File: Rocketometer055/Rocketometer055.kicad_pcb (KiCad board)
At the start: 2 copper layers, 26.7 x 20.3 mm, 31 parts, among them Q1 BSS138, Q2 BSS138, U1 MIC5225, Y1 32.768kHz

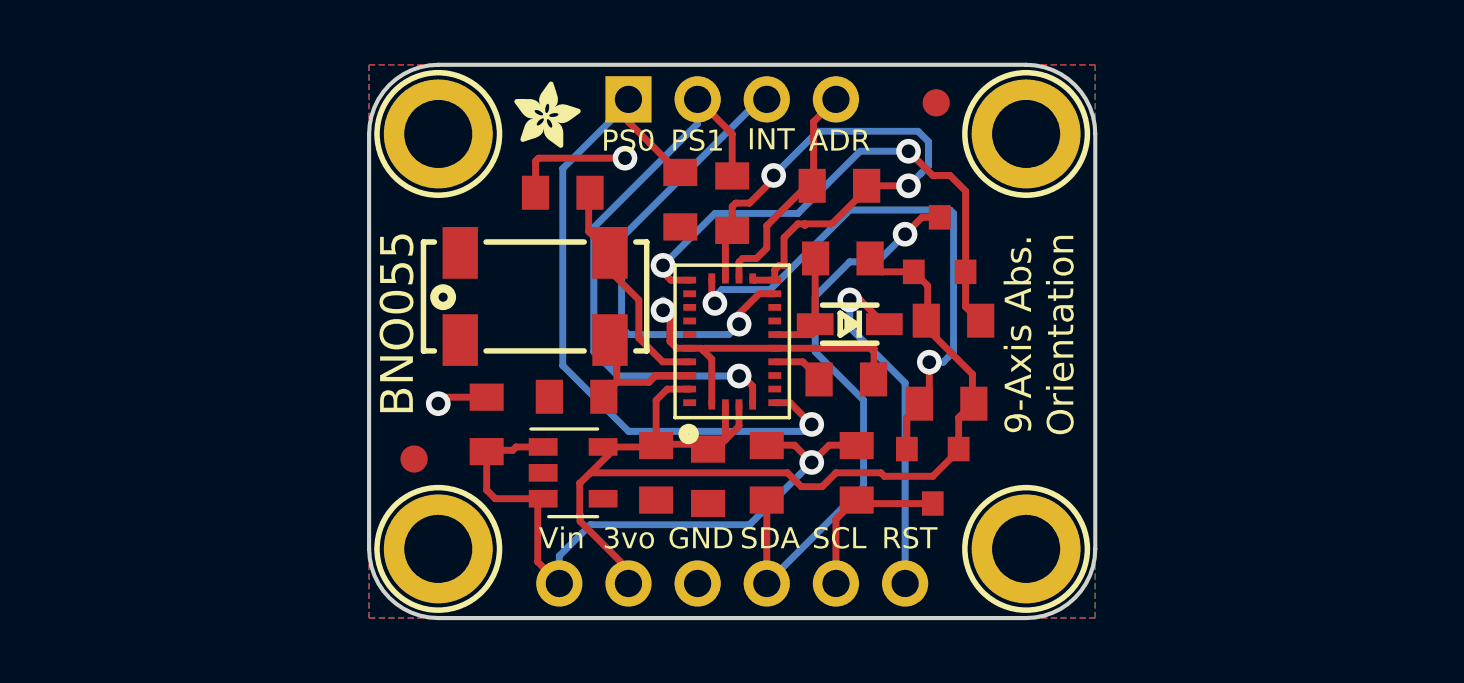
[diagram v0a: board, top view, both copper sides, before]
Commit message: Importing Rocketometer6050 as flown
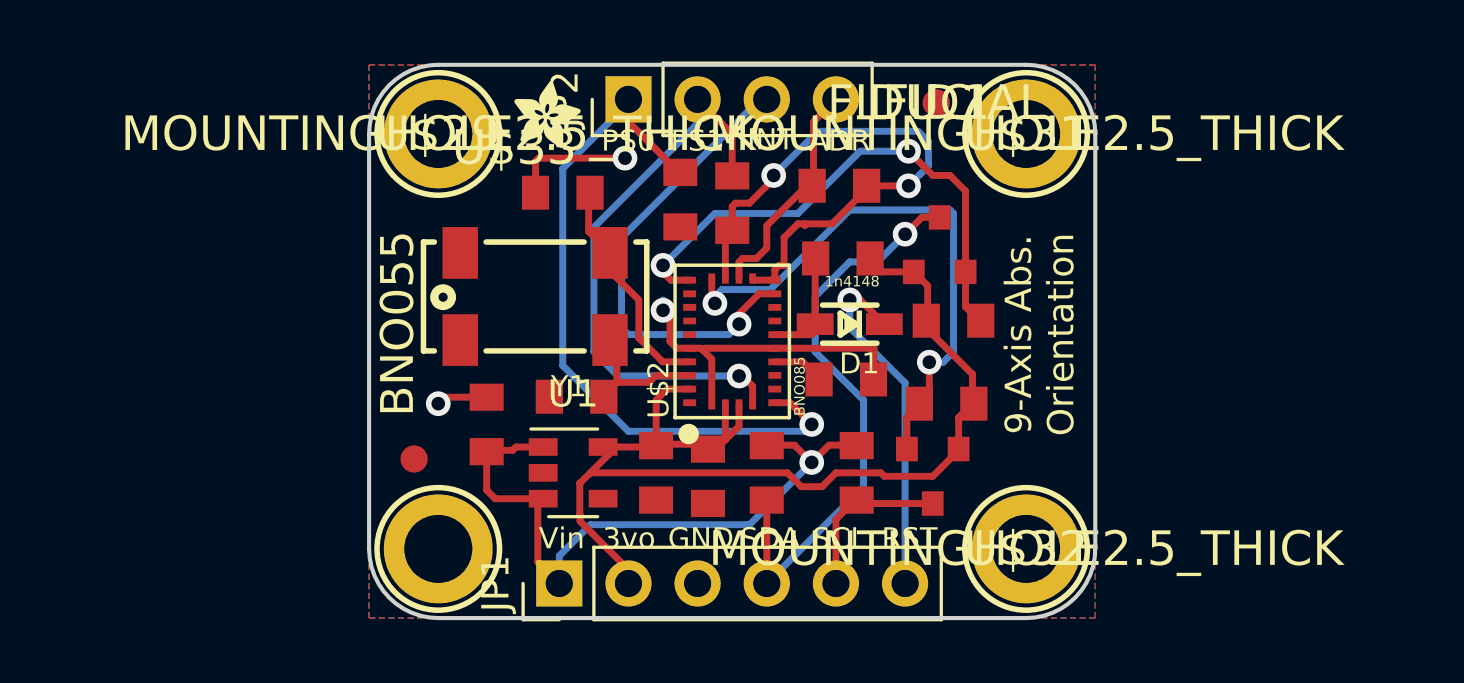
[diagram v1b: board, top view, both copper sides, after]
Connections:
- net /BMO055/N$1 renamed /N$1
- net /BMO055/N$2 renamed /N$2
- net /BMO055/N$3 renamed /N$3
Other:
- net class Default: clearance 0 -> 0.1524
- rule trace_clearance: 0 -> 0.1524

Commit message: Worked on Rocketometer055
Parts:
- removed C1, C2: 22pF, KwanSystems:SMD_0805
- removed C3, C4: 0.1uF, KwanSystems:SMD_0805
- removed C5, C6: 10uF, KwanSystems:SMD_0805
- removed D1: 1n4148, KwanSystems:SOD-323
- removed FID1, FID2: FIDUCIAL, FIDUCIAL_1MM
- removed Q1, Q2: BSS138, KwanSystems:SOT-23
- removed R10, R3, R4, R5, R6, R7, R8, R9: 10K, KwanSystems:SMD_0805
- removed U$2: BNO085, KwanSystems:BNO055
- removed U$28: , ADAFRUIT_TEXT_20MM
- removed U$29, U$30, U$31, U$32: MOUNTINGHOLE2.5_THICK, MOUNTINGHOLE_2.5_PLATED_THICK
- removed U$3: , PCBFEAT-REV-040
- removed U$33: , ADAFRUIT_2.5MM
- removed U1: MIC5225, TO_SOT_Packages_SMD:SOT-23-5
- removed Y1: 32.768kHz, KwanSystems:CRYSTAL_8X3.8
- added B504: Coin_Cell, KwanSystems:CR1220-2, F.Cu at (164.1, 91.7)
- added C010: 1uF, KwanSystems:SMD_0402, F.Cu at (264.9, 116.1)
- added C020: 22pF, KwanSystems:SMD_0402, F.Cu at (258.5, 114.4)
- added C023: 22pF, KwanSystems:R_Array_Convex_2x0402, F.Cu at (176.9, 85.3)
- added C030: 22pF, KwanSystems:SMD_0402, F.Cu at (260.9, 111.0)
- added C106: 100nF, KwanSystems:R_Array_Convex_2x0402, F.Cu at (150.1, 83.7)
- added C204: 1uF, KwanSystems:SMD_0402, F.Cu at (253.0, 110.7)
- added C214: 100nF, KwanSystems:SMD_0402, F.Cu at (252.5, 121.5)
- added C215: 4.7nF, KwanSystems:SMD_0402, F.Cu at (249.0, 123.1)
- added C302: 4.7uF, KwanSystems:SMD_0603, F.Cu at (253.5, 114.3)
- added C303: 4.7uF, KwanSystems:SMD_0603, F.Cu at (175.0, 96.3)
- added C423: 1uF, KwanSystems:SMD_0402, B.Cu at (157.0, 100.8)
- added C443: 100nF, KwanSystems:SMD_0402, B.Cu at (149.9, 93.0)
- added C451: 100nF, KwanSystems:SMD_0402, B.Cu at (152.7, 87.0)
- added C461: 33pF, KwanSystems:SMD_0402, B.Cu at (158.5, 82.8)
- added C462: 33pF, KwanSystems:SMD_0402, B.Cu at (161.8, 85.6)
- added C463: 100nF, KwanSystems:SMD_0402, B.Cu at (162.1, 88.1)
- added C501: 100nF, KwanSystems:SMD_0402, F.Cu at (171.5, 136.9)
- added C503: 10uF, KwanSystems:SMD_1206, F.Cu at (187.3, 124.7)
- added C504: 220mF, KwanSystems:Supercap, F.Cu at (212.4, 114.1)
- added C603: 0.1uF, KwanSystems:SMD_0402, F.Cu at (174.7, 147.7)
- added C609: 0.1uF, KwanSystems:SMD_0402, F.Cu at (170.2, 148.6)
- added C626: 22pF, KwanSystems:SMD_0402, F.Cu at (155.2, 91.4)
- added C627: 22pF, KwanSystems:SMD_0402, F.Cu at (155.4, 87.4)
- added C901: 100nF, KwanSystems:SMD_0402, F.Cu at (184.5, 142.1)
- added C914: 100nF, KwanSystems:SMD_0402, F.Cu at (184.5, 143.3)
- added C916: 1uF, KwanSystems:SMD_0402, F.Cu at (186.9, 142.1)
- added D050: BLUE, KwanSystems:D_0603, F.Cu at (179.6, 85.3)
- added D301: YELLOW, KwanSystems:D_0603, F.Cu at (249.5, 121.7)
- added D302: DCC, KwanSystems:SOT-23, F.Cu at (175.0, 93.7)
- added D401: HSMF-C118, KwanSystems:HSMF-C118, B.Cu at (167.1, 81.8)
- added D504: D_Schottky, KwanSystems:D_0603, F.Cu at (168.3, 137.1)
- added J001: USB_MICROB, KwanSystems:USB_Micro-B_Molex_47346-0001, F.Cu at (182.9, 90.2)
- added J301: JST 2mm, Connectors_JST:JST_PH_S2B-PH-SM4-TB_02x2.00mm_Angled, B.Cu at (178.3, 90.2)
- added J401: ~, Pin_Headers:Pin_Header_Straight_1x10_Pitch2.54mm, F.Cu at (163.8, 80.0)
- added J701: Micro_SD_Card_Det_Hirose_DM3AT, KwanSystems:MICROSD-SOCKET-PP, F.Cu at (132.6, 84.2)
- added JP4: STAND-OFFTIGHT, STAND-OFF-TIGHT, F.Cu at (180.3, 99.1)
- added JP5: STAND-OFFTIGHT, STAND-OFF-TIGHT, F.Cu at (180.3, 81.3)
- added L501: Ferrite, KwanSystems:SMD_0805, F.Cu at (175.7, 130.1)
- added Q050: PMOS, KwanSystems:SOT-23, F.Cu at (174.2, 84.1)
- added R010: 10k, KwanSystems:SMD_0402, F.Cu at (177.8, 95.5)
- added R011: 22k, KwanSystems:SMD_0402, F.Cu at (254.8, 121.5)
- added R023: 33, KwanSystems:R_Array_Convex_2x0402, F.Cu at (176.9, 87.4)
- added R050: 1.5k, KwanSystems:R_Array_Convex_2x0402, F.Cu at (176.9, 83.3)
- added R051: 10k, KwanSystems:SMD_0402, F.Cu at (251.4, 123.9)
- added R301: 10k, KwanSystems:SMD_0402, F.Cu at (254.8, 122.7)
- added R302: 1.5k, KwanSystems:SMD_0402, F.Cu at (253.5, 113.0)
- added R304: 1.5k, KwanSystems:SMD_0402, F.Cu at (177.8, 96.5)
- added R401: 10k, KwanSystems:R_Array_Convex_4x0402, B.Cu at (151.9, 85.1)
- added R402: 1.5k, KwanSystems:R_Array_Convex_4x0402, B.Cu at (169.7, 81.8)
- added R504: 10k, KwanSystems:SMD_0402, F.Cu at (206.3, 122.8)
- added R914: 100, KwanSystems:SMD_0402, F.Cu at (186.9, 143.3)
- added S201: SPDT, KwanSystems:SWITCH_DPDT_AZY0202, B.Cu at (172.5, 97.8)
- added S456: SOLDERJUMPERNO, Connectors:GS2, B.Cu at (155.3, 82.8)
- added S457: SPST, KwanSystems:SW_SPST_B3U-1000P, B.Cu at (155.4, 85.6)
- added U101: BME280, KwanSystems:BME280, F.Cu at (152.7, 83.9)
- added U201: 3.3V, TO_SOT_Packages_SMD:SOT-23-5, F.Cu at (250.0, 110.8)
- added U301: MCP73831, TO_SOT_Packages_SMD:SOT-23-5, F.Cu at (175.0, 90.2)
- added U401: LPC2148, Housings_QFP:LQFP-64_10x10mm_Pitch0.5mm, B.Cu at (156.8, 93.9)
- added U501: FGPMMOPA6H, KwanSystems:FGPMMOPA6H, B.Cu at (140.5, 90.6)
- added U501: MPU9250, KwanSystems:Axis, F.Cu at (175.3, 100.3)
- added U601: BNO085, KwanSystems:BNO055, F.Cu at (152.4, 90.2)
- added U901: ADXL375, KwanSystems:ADXL375, F.Cu at (153.3, 98.4)
- added X511: uFL, KwanSystems:U.FL, B.Cu at (129.5, 92.5)
- added Y401: 12MHz, Crystals:Crystal_SMD_Abracon_ABM8G-4pin_3.2x2.5mm, B.Cu at (159.4, 85.5)
- added Y601: 32kiHz, Crystals:Crystal_SMD_2012-2pin_2.0x1.2mm, F.Cu at (155.2, 89.2)
- JP1: value ~ -> STAND-OFFTIGHT; footprint Pin_Headers:Pin_Header_Straight_1x06_Pitch2.54mm -> STAND-OFF-TIGHT
- JP2: value ~ -> STAND-OFFTIGHT; footprint Pin_Headers:Pin_Header_Straight_1x04_Pitch2.54mm -> STAND-OFF-TIGHT
- moved JP2 7.10 mm to (129.5, 81.3), turned to 0 degrees
- moved JP1 4.62 mm to (129.5, 99.1), turned to 0 degrees
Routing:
- net GND: track 41.0 -> 0.00 mm, vias 5 -> 0
- net +3V3: track 40.6 -> 0.00 mm
- net /PS0_3V: track 26.2 -> 0.00 mm, vias 1 -> 0
- net +5V: track 24.4 -> 0.00 mm, vias 1 -> 0
- net /SDA_5V: track 21.6 -> 0.00 mm, vias 1 -> 0
- net /PS1_3V: track 21.3 -> 0.00 mm, vias 1 -> 0
- net /SCL_3V: track 21.2 -> 0.00 mm, vias 2 -> 0
- net /SDA_3V: track 19.8 -> 0.00 mm, vias 2 -> 0
- net /INT_3V: track 17.3 -> 0.00 mm, vias 1 -> 0
- net VCC: track 0.00 -> 16.7 mm
- net /RST_5V: track 12.9 -> 0.00 mm, vias 1 -> 0
- net /I2CADDR_3V: track 8.50 -> 0.00 mm
- net /N$2: track 8.33 -> 0.00 mm
- net /RST: track 0.00 -> 8.02 mm
- net /CONN_D+: track 0.00 -> 7.92 mm
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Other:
- board size 26.7 x 20.3 mm -> 55.9 x 22.9 mm
- board text added: "3V3"
- board text added: "BSL"
- board text added: "Baro"
- board text added: "D"
- board text added: "HighAcc"
- board text added: "Kwan Systems"
- board text added: "On"
- board text added: "RX0"
- board text added: "Reset"
- board text added: "RocketometerBNO055"
- board text added: "St Kwan's Home for"
- board text added: "TX0"
- board text added: "VBUS"
- board text added: "a division of"
- board text added: "stkwans.blogspot.com"
- board text added: "the Terminally ADD"
- board text added: "v1.0 19 Nov 2012"
- board text removed: "3-Axis Accel+Gyro+Mag w/Quaternion, Euler Heading, etc. I2C Out"
- board text removed: "3vo"
- board text removed: "9-Axis Abs. Orientation"
- board text removed: "ADR"
- board text removed: "BNO055"
- board text removed: "INT"
- board text removed: "PS0"
- board text removed: "PS1"
- board text removed: "RST"
- board text removed: "Vin"
- board text removed: "Vin:3-5V DC, 3V logic SDA/SCL/RST: 5V ok"

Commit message: Worked on Rocketometer055
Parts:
- removed C504: 220mF, KwanSystems:Supercap
- removed D504: D_Schottky, KwanSystems:D_0603
- removed R504: 10k, KwanSystems:SMD_0402
- moved C501 63.0 mm to (129.5, 89.9)
- moved L501 62.9 mm to (129.5, 87.4)
- moved C603 46.7 mm to (188.7, 103.1)
- moved C609 46.3 mm to (184.1, 104.4)

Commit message: More work on Rocketometer055
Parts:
- removed C010: 1uF, KwanSystems:SMD_0402
- removed C020, C030: 22pF, KwanSystems:SMD_0402
- removed R010: 10k, KwanSystems:SMD_0402
- D401: footprint KwanSystems:HSMF-C118 -> HSMF-C118
- J701: footprint KwanSystems:MICROSD-SOCKET-PP -> MICROSD-SOCKET-PP
- R051: footprint KwanSystems:SMD_0402 -> KwanSystems:R_Array_Convex_2x0402
- moved R011 79.5 mm to (179.8, 95.0), turned to 180 degrees
- moved R051 79.0 mm to (177.8, 95.2)
- moved D301 73.8 mm to (180.3, 96.0), turned to 180 degrees
- moved C503 67.3 mm to (129.4, 90.4)
- moved C901 66.1 mm to (151.0, 85.1)
- moved R906 60.2 mm to (151.6, 94.5), turned to 180 degrees
- moved C906 58.6 mm to (151.6, 95.2)
- moved C905 57.6 mm to (151.6, 96.0)
- moved U501 49.4 mm to (127.8, 86.7)
- moved C603 39.9 mm to (152.1, 87.0)
- moved C609 37.3 mm to (149.9, 89.7), turned to 90 degrees
- moved C215 13.2 mm to (253.5, 110.7), turned to 270 degrees
- moved C214 10.7 mm to (252.5, 110.7), turned to 90 degrees
- moved R302 8.21 mm to (256.5, 120.7)
- moved C302 5.86 mm to (253.0, 120.1)
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- renumbered C914 to C905, C916 to C906, R914 to R906
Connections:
- net /TX0/PWMR renamed /TX0(PWMR)
- net Net-(C914-Pad1) renamed /HighAcc/VS
- J401 pad 7: (no net) -> /SDA(BSL)
- J401 pad 8: (no net) -> /SCL
- R051 pad 1: /USB_SOFTCONNECT -> /VBUS
- R401 pad 1: /SDA/BSL -> /SDA(BSL)
- U101 pad 3: /SDA/BSL -> /SDA(BSL)
- U401 pad 41: /SDA/BSL -> /SDA(BSL)
- U601 pad 20: /SDA/BSL -> /SDA(BSL)
- U901 pad 13: /SDA/BSL -> /SDA(BSL)
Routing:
- net VCC: track 16.7 -> 29.1 mm
- net /TX0(PWMR): track 0.00 -> 10.9 mm, vias 0 -> 2
- net /VBUS: track 4.82 -> 9.96 mm
- net /VLIPO: track 5.47 -> 9.09 mm
- net /HighAcc/VS: track 0.00 -> 2.89 mm
- net /VIN: track 0.00 -> 2.14 mm, vias 0 -> 1
- net /STAT+: track 0.00 -> 1.40 mm
- net /BNO055/CAP: track 0.00 -> 1.11 mm
- net /USB_ON: track 0.00 -> 1.02 mm
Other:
- board text added: "v1.0 19 Nov 2017"
- board text removed: "HighAcc"
- board text removed: "Reset"
- board text removed: "St Kwan's Home for"
- board text removed: "a division of"
- board text removed: "the Terminally ADD"
- board text removed: "v1.0 19 Nov 2012"

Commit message: First complete routing of Rocketometer
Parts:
- removed R302: 1.5k, KwanSystems:SMD_0402
- C204, C214, C215, C501, U201: moved to B.Cu
- C423, S456: moved to F.Cu
- J701: footprint MICROSD-SOCKET-PP -> KwanSystems:MICROSD-SOCKET-PP
- moved R301 88.0 mm to (174.5, 86.9)
- moved C302 83.1 mm to (175.0, 91.4), turned to 180 degrees
- moved C215 80.1 mm to (178.1, 83.8)
- moved C214 79.9 mm to (177.3, 83.8), turned to 270 degrees
- moved U201 79.7 mm to (175.0, 83.8)
- moved C204 79.6 mm to (172.7, 83.8), turned to 90 degrees
- moved C501 22.2 mm to (149.6, 85.3), turned to 90 degrees
- moved C901 11.5 mm to (154.7, 96.0), turned to 180 degrees
- moved C461 3.07 mm to (157.2, 85.6), turned to 270 degrees
- moved S456 3.06 mm to (157.5, 85.0), turned to 180 degrees
- moved C303 3.05 mm to (175.0, 93.2)
- moved D401 1.98 mm to (168.7, 80.6), turned to 0 degrees
- moved D302 1.76 mm to (175.0, 95.5)
- moved R402 1.65 mm to (168.8, 83.2), turned to 270 degrees
- moved U301 1.28 mm to (174.3, 89.1)
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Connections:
- J401 pad 1: /VBUS -> /RST
- J401 pad 10: VCC -> /GPS_TX
- J401 pad 4: /GPS_RX -> /VBUS
- J401 pad 5: /GPS_TX -> /SDA(BSL)
- J401 pad 7: /SDA(BSL) -> /SCL
- J401 pad 8: /SCL -> VCC
- J401 pad 9: (no net) -> /GPS_RX
- J701 pad 10: (no net) -> GND
- U401 pad 15: /FIX -> (no net)
- U401 pad 17: (no net) -> /USB_SOFTCONNECT
- U401 pad 35: (no net) -> /FIX
- U901 pad 12: (no net) -> GND
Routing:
- net VCC: track 29.1 -> 155.3 mm, vias 0 -> 13
- net GND: track 0.00 -> 93.6 mm, vias 0 -> 22
- net /USB_SOFTCONNECT: track 0.05 -> 41.6 mm, vias 0 -> 2
- net /SCL: track 0.00 -> 38.7 mm, vias 0 -> 6
- net /VBUS: track 9.96 -> 48.5 mm, vias 0 -> 3
- net /PPS: track 0.00 -> 35.1 mm, vias 0 -> 2
- net /SDA(BSL): track 0.00 -> 31.8 mm, vias 0 -> 2
- net /PWMG: track 0.00 -> 30.9 mm, vias 0 -> 2
- net /USB_ON: track 1.02 -> 31.9 mm, vias 0 -> 1
- net /TX0(PWMR): track 10.9 -> 38.9 mm
- net /USBD-: track 1.03 -> 28.7 mm, vias 0 -> 1
- net /GPS_TX: track 0.00 -> 26.7 mm, vias 0 -> 1
- net /PWR_EN: track 0.00 -> 26.3 mm, vias 0 -> 2
- net /GPS_RX: track 0.00 -> 25.9 mm, vias 0 -> 1
- net /GPS/VGPS: track 0.00 -> 25.5 mm, vias 0 -> 1
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
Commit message: Modular hardware, just before redoing the main board
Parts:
- J801: renamed from J301; footprint Connectors_JST:JST_PH_S2B-PH-SM4-TB_02x2.00mm_Angled -> KwanSystems:SPARKFUN_JST_POWER
- moved S156 1.73 mm to (158.5, 83.6), turned to 270 degrees
- renumbered C423 to C123, C443 to C143, C451 to C151, C461 to C161, C462 to C162, C463 to C163, C106 to C206, C603 to C303, C609 to C309, C626 to C326, C627 to C327, C901 to C401, C905 to C405, C906 to C406, C023 to C623, C204 to C704, C214 to C714, C215 to C715, C302 to C802, C303 to C803, D401 to D101, D050 to D650, D301 to D801, D302 to D802, J401 to J101, J701 to J102, J001 to J601, Q050 to Q650, R401 to R101, R402 to R102, R906 to R406, R011 to R611, R023 to R623, R050 to R650, R051 to R651, R301 to R801, R304 to R804, S456 to S156, S457 to S157, S201 to S701, U401 to U101, U101 to U201, U601 to U301, U901 to U401, U201 to U701, U301 to U801, Y401 to Y101, Y601 to Y301
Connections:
- net /BYP renamed /Regulator/BYP
- net /CONN_D+ renamed /USB/CONN_D+
- net /CONN_D- renamed /USB/CONN_D-
- net /PROG renamed /Charger/PROG
- net /PWR_EN renamed /Regulator/PWR_EN
- net /STAT+ renamed /Charger/STAT+
- net /STAT- renamed /Charger/STAT-
- net /USB_LIGHT+ renamed /USB/USB_LIGHT+
- net /USB_LIGHT- renamed /USB/USB_LIGHT-
- net /VIN renamed /VRAW
- C803 pad 1: /VLIPO -> /Charger/VLIPO
- D802 pad 2: /VLIPO -> /Charger/VLIPO
- J102 pad 1: (no net) -> Net-(J102-Pad1)
- J102 pad 8: (no net) -> Net-(J102-Pad8)
- J601 pad 4: (no net) -> Net-(J601-Pad4)
- U101 pad 12: (no net) -> Net-(U101-Pad12)
- U101 pad 13: (no net) -> Net-(U101-Pad13)
- U101 pad 14: (no net) -> Net-(U101-Pad14)
- U101 pad 15: (no net) -> Net-(U101-Pad15)
- U101 pad 16: (no net) -> Net-(U101-Pad16)
- U101 pad 20: (no net) -> Net-(U101-Pad20)
- U101 pad 22: (no net) -> Net-(U101-Pad22)
- U101 pad 24: (no net) -> Net-(U101-Pad24)
- U101 pad 26: (no net) -> Net-(U101-Pad26)
- U101 pad 28: (no net) -> Net-(U101-Pad28)
- U101 pad 3: (no net) -> Net-(U101-Pad3)
- U101 pad 32: (no net) -> Net-(U101-Pad32)
- U101 pad 36: (no net) -> Net-(U101-Pad36)
- U101 pad 38: (no net) -> Net-(U101-Pad38)
- U101 pad 39: (no net) -> Net-(U101-Pad39)
- U101 pad 4: (no net) -> Net-(U101-Pad4)
- U101 pad 40: (no net) -> Net-(U101-Pad40)
- U101 pad 44: (no net) -> Net-(U101-Pad44)
- U101 pad 47: (no net) -> Net-(U101-Pad47)
- U101 pad 48: (no net) -> Net-(U101-Pad48)
- U101 pad 5: (no net) -> Net-(U101-Pad5)
- U101 pad 52: (no net) -> Net-(U101-Pad52)
- U101 pad 53: (no net) -> Net-(U101-Pad53)
- U101 pad 54: (no net) -> Net-(U101-Pad54)
- U101 pad 55: (no net) -> Net-(U101-Pad55)
- U101 pad 56: (no net) -> Net-(U101-Pad56)
- U101 pad 60: (no net) -> Net-(U101-Pad60)
- U101 pad 64: (no net) -> Net-(U101-Pad64)
- U101 pad 8: (no net) -> Net-(U101-Pad8)
- U101 pad 9: (no net) -> Net-(U101-Pad9)
- U301 pad 7: (no net) -> Net-(U301-Pad7)
- U301 pad 8: (no net) -> Net-(U301-Pad8)
- U401 pad 8: (no net) -> /HighAcc/INT
- U501 pad 14: (no net) -> Net-(U501-Pad14)
- U501 pad 2: (no net) -> Net-(U501-Pad2)
- U801 pad 3: /VLIPO -> /Charger/VLIPO
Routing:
- net /VLIPO: track 9.35 -> 0.00 mm, vias 1 -> 0
- net /Charger/VLIPO: track 0.00 -> 9.07 mm, vias 0 -> 1
- net GND: track 93.6 -> 90.8 mm
- net /RX0: track 25.5 -> 26.7 mm
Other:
- board text added: "BUS"
- board text added: "RST"
- board text added: "RXG"
- board text added: "TXG"
- board text removed: "Baro"
- board text removed: "SDA"
- board text removed: "VBUS"
